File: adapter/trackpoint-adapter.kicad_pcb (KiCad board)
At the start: 2 copper layers, 23 x 18 mm, 5 parts

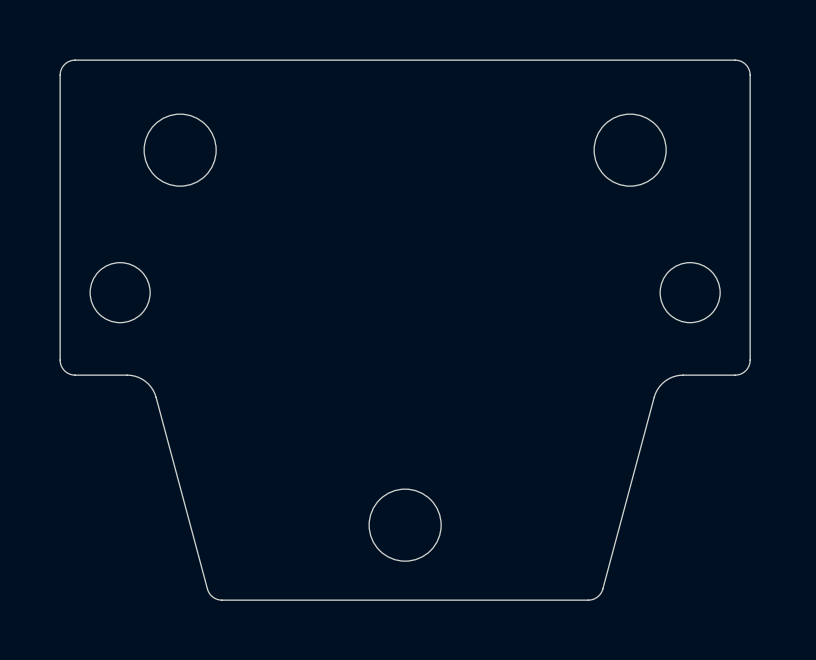
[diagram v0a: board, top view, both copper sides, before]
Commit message: Add version number and PCB ID for the adapter board.
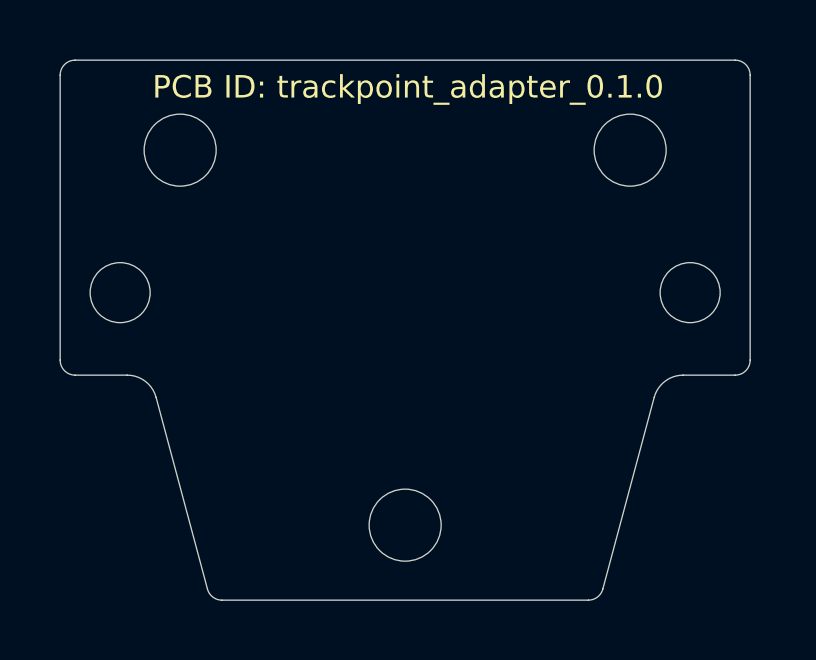
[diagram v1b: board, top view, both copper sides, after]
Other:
- board text added: "PCB ID: trackpoint_adapter_0.1.0"
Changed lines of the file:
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@@
   (general
     (thickness 1.6)
-    (drawings 16)
+    (drawings 17)
     (tracks 0)
     (zones 0)
@@
   )
   (page A3)
+  (title_block
+    (title "UHK Trackpoint Module - Adapter")
+    (rev 0.1.0)
+    (company "Ultimate Gadget Laboratories Kft.")
+  )
   (layers
     (0 F.Cu signal)
@@
       (clearance 0.00001))
   )
+  (gr_text "PCB ID: trackpoint_adapter_0.1.0" (at 206.1 141.4) (layer F.SilkS)
+    (effects (font (size 0.75 0.75) (thickness 0.15)))
+  )
   (gr_arc (start 199.893278 158.000006) (end 199.41032 158.12941) (angle -75.00591082) (layer Edge.Cuts) (width 0.01))
